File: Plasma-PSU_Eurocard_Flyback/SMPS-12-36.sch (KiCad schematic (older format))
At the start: 49 parts, among them Q501 NVTFS6H850NL, Q502 NVTFS6H850NL, U501 MCP602, U502 MCP602, U503 LTC3786, U504 MCP4822

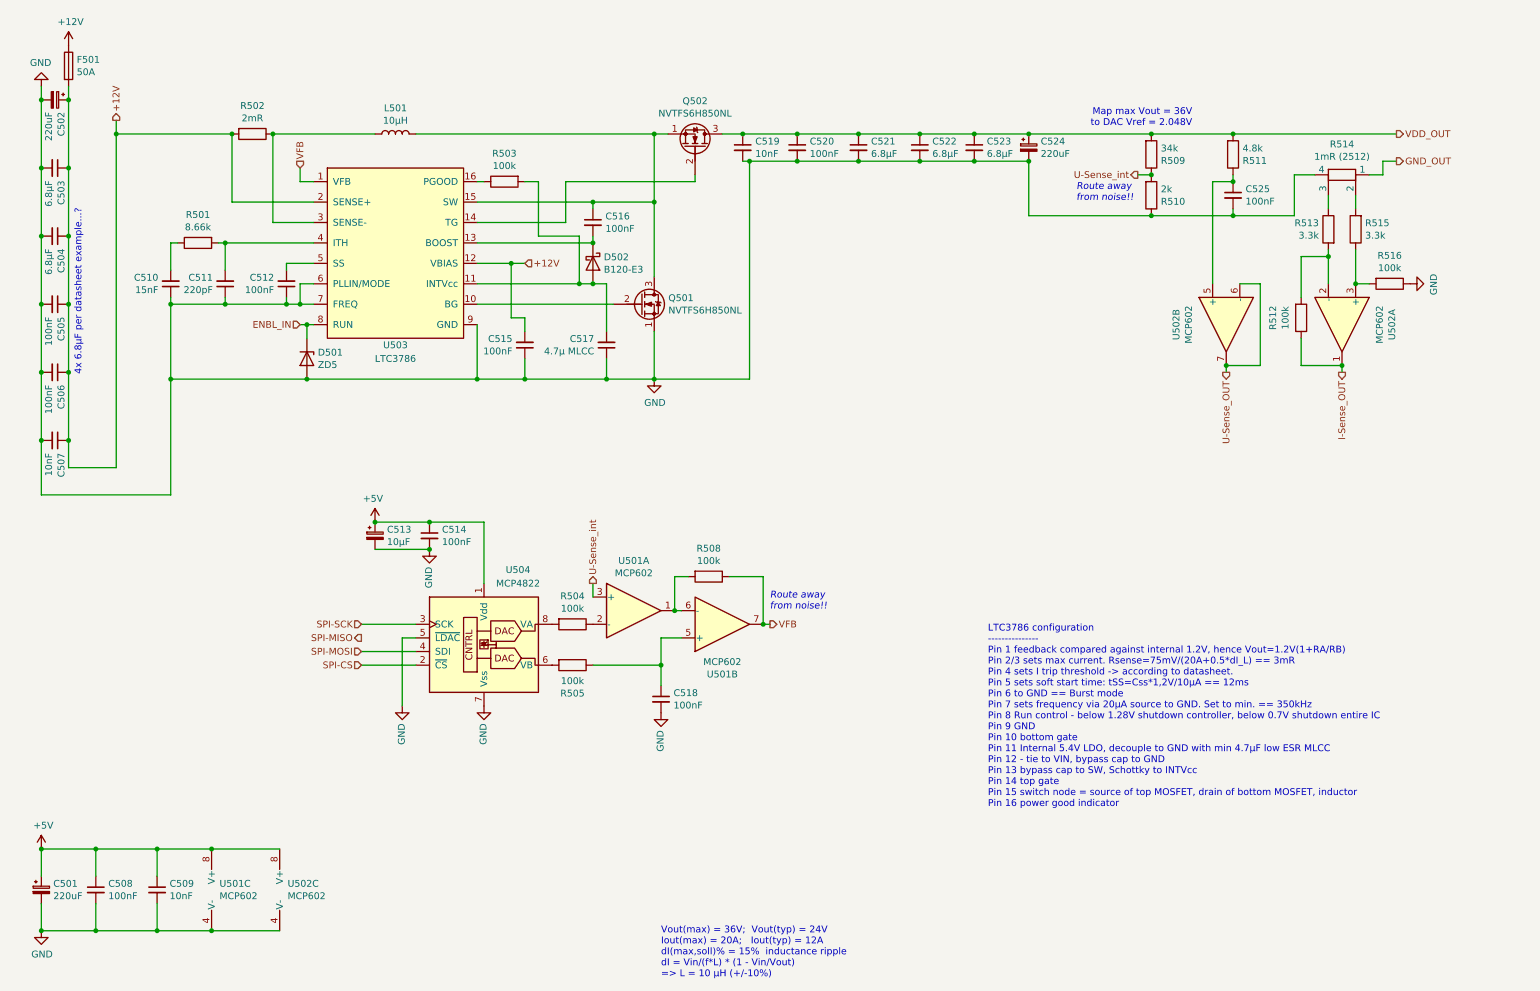
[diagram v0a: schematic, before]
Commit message: Testpoints & SMPS jumper included
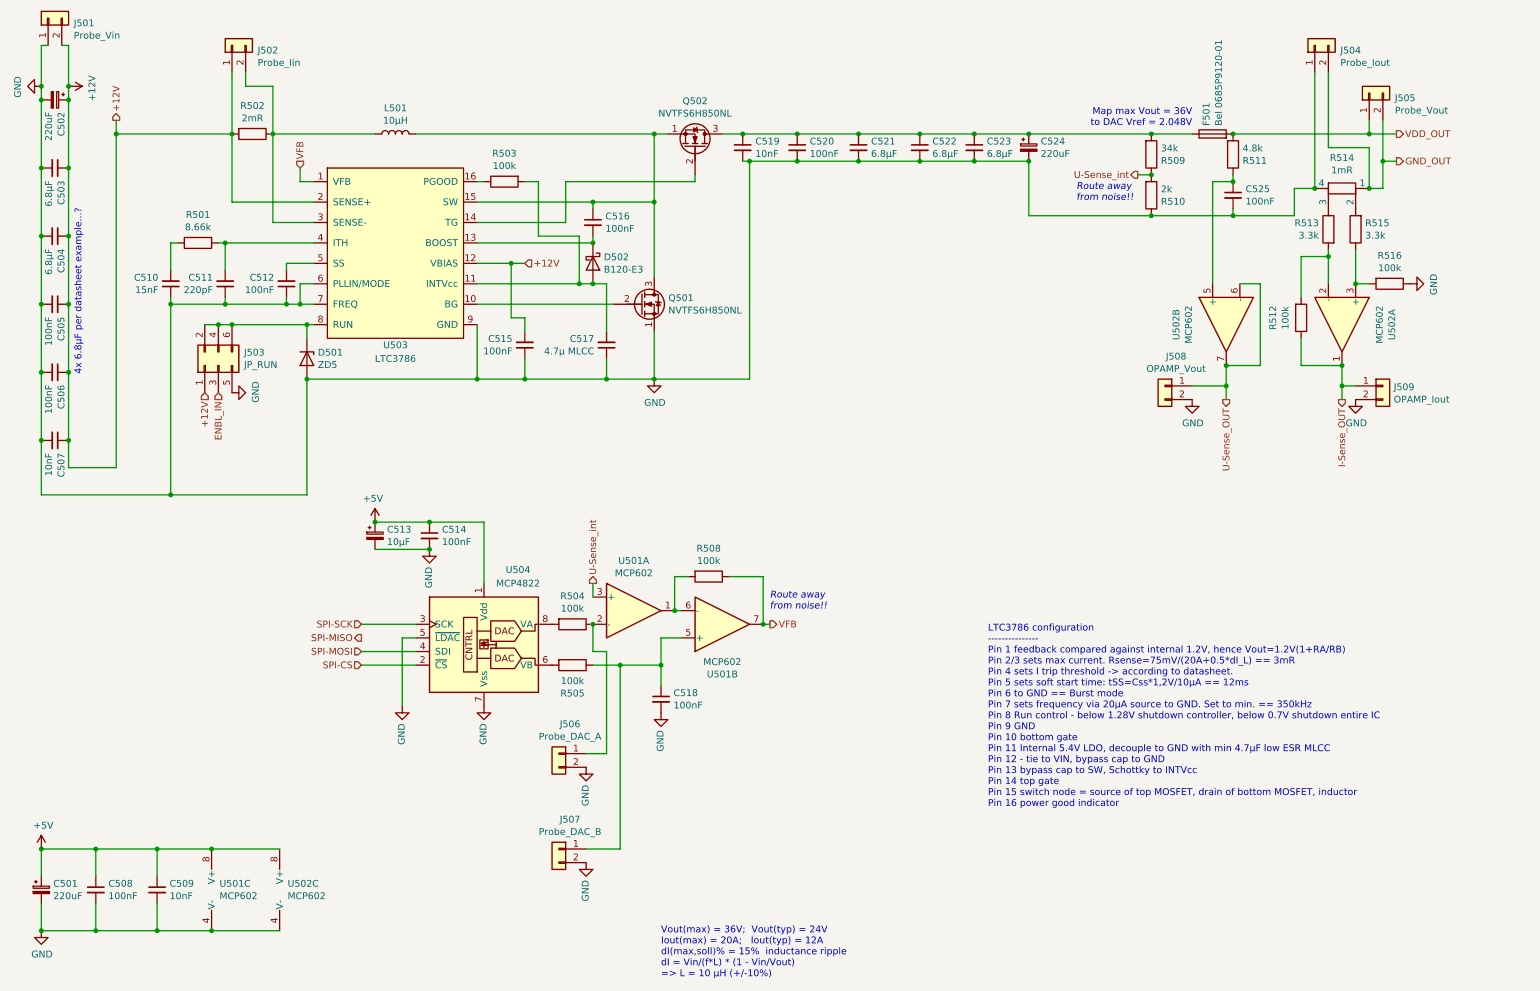
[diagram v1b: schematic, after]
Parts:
- added J501: Probe_Vin, TestPoint:TestPoint_2Pads_Pitch5.08mm_Drill1.3mm, symbol Connector_Generic:Conn_01x02
- added J502: Probe_Iin, TestPoint:TestPoint_2Pads_Pitch5.08mm_Drill1.3mm, symbol Connector_Generic:Conn_01x02
- added J503: JP_RUN, Connector_PinHeader_2.54mm:PinHeader_2x03_P2.54mm_Vertical, symbol Connector_Generic:Conn_02x03_Odd_Even
- added J504: Probe_Iout, TestPoint:TestPoint_2Pads_Pitch5.08mm_Drill1.3mm, symbol Connector_Generic:Conn_01x02
- added J505: Probe_Vout, TestPoint:TestPoint_2Pads_Pitch5.08mm_Drill1.3mm, symbol Connector_Generic:Conn_01x02
- added J506: Probe_DAC_A, TestPoint:TestPoint_2Pads_Pitch5.08mm_Drill1.3mm, symbol Connector_Generic:Conn_01x02
- added J507: Probe_DAC_B, TestPoint:TestPoint_2Pads_Pitch5.08mm_Drill1.3mm, symbol Connector_Generic:Conn_01x02
- added J508: OPAMP_Vout, TestPoint:TestPoint_2Pads_Pitch5.08mm_Drill1.3mm, symbol Connector_Generic:Conn_01x02
- added J509: OPAMP_Iout, TestPoint:TestPoint_2Pads_Pitch5.08mm_Drill1.3mm, symbol Connector_Generic:Conn_01x02
- F501: value 50A -> Bel 0685P9120-01; footprint (none) -> Fuse:Fuse_1206_3216Metric_Pad1.42x1.75mm_HandSolder
- R514: value 1mR (2512) -> 1mR
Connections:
- net +12V: now also J501.2 (Pin_2), J502.1 (Pin_1), J503.1 (Pin_1); no longer F501.1, F501.2
- net ENBL_IN: now also J503.3 (Pin_3); no longer D501.1 (K), U503.8 (RUN)
- net GND: now also J501.1 (Pin_1), J503.5 (Pin_5), J504.1 (Pin_1), J506.2 (Pin_2), J507.2 (Pin_2), J508.2 (Pin_2), J509.2 (Pin_2)
- net GND_OUT: now also J504.2 (Pin_2), J505.2 (Pin_2)
- net I-Sense_OUT: now also J509.1 (Pin_1)
- net U-Sense_OUT: now also J508.1 (Pin_1)
- net VDD_OUT: now also F501.2, J505.1 (Pin_1); no longer C519.1, C520.1, C521.1, C522.1, C523.1, C524.1, Q502.3 (D), R509.2
- net at C518.1, R505.1, U501.5 (+): now also J507.1 (Pin_1)
- net at L501.1, R502.1, U503.3 (SENSE-): now also J502.2 (Pin_2)
- net at R504.1, U501.2 (-): now also J506.1 (Pin_1)
- new net: C519.1, C520.1, C521.1, C522.1, C523.1, C524.1, F501.1, Q502.3 (D), R509.2
- new net: D501.1 (K), J503.2 (Pin_2), J503.4 (Pin_4), J503.6 (Pin_6), U503.8 (RUN)
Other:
- moved on the sheet: F501, R514
